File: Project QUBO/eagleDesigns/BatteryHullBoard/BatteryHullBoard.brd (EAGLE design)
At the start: 53.3 x 39.7 mm, 7 parts, among them U1 KSK-1E66, U2 CMXSIPSSR

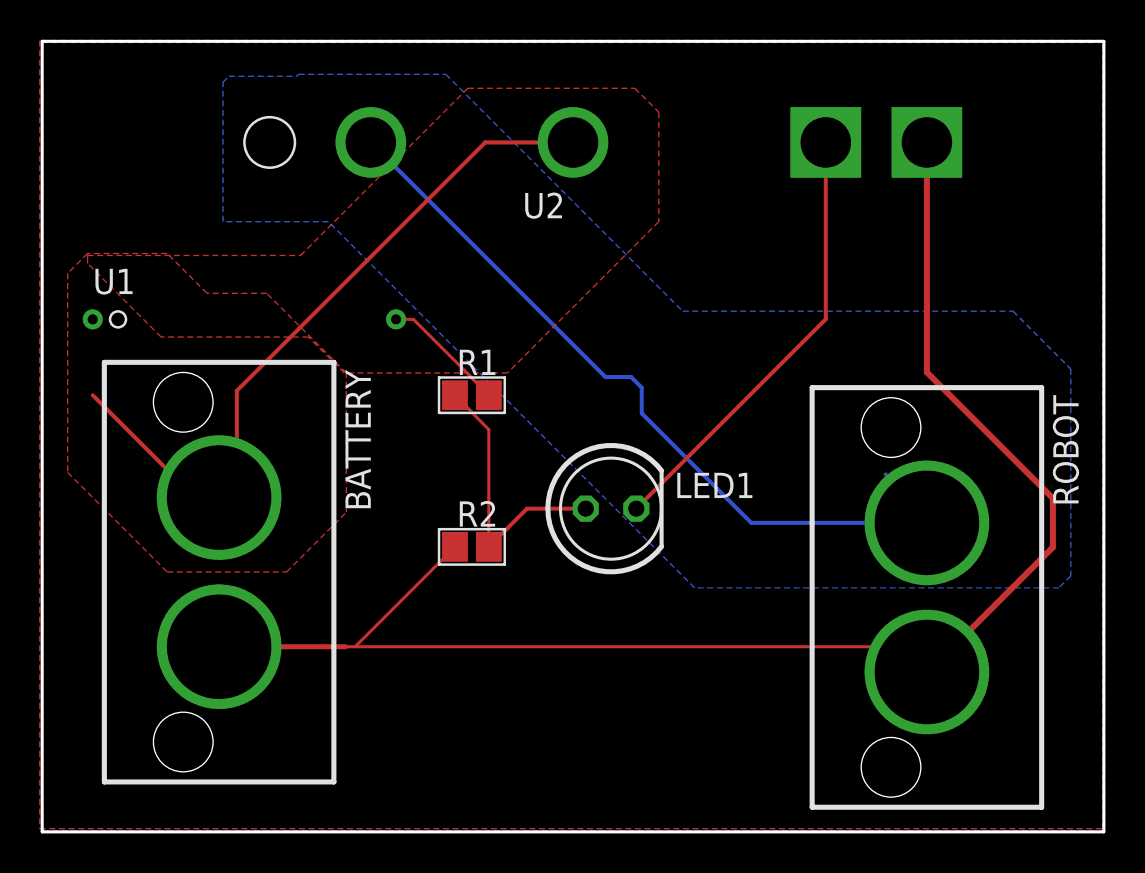
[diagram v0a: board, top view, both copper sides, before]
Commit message: 
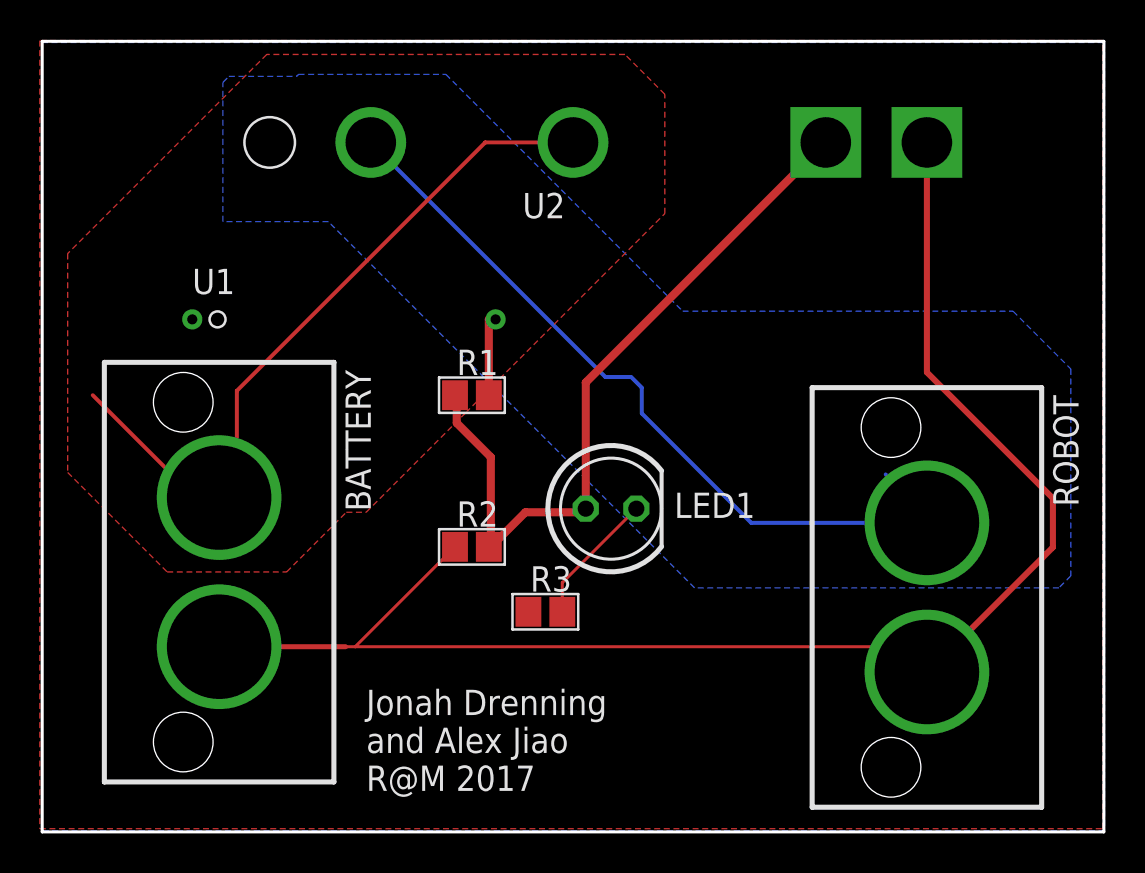
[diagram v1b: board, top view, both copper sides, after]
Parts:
- added R3: 10000, resistor:R0805
- moved U1 5.00 mm to (60.9, 59.7)
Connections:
- removed net N$6: LED1.K, U2.P$3
- new net N$4: LED1.K, R3.2
- net GND: now also R3.1
- net N$3: now also U2.P$3
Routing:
- net N$3: track 14.0 -> 37.4 mm
- net N$6: track 22.3 -> 0.00 mm
- net N$4: track 0.00 -> 6.72 mm
- net N$1: track 6.25 -> 4.15 mm
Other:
- board text added: "Jonah Drenning and Alex Jiao R@M 2017"
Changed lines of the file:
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@@
 <wire x1="45.72" y1="73.66" x2="99.06" y2="73.66" width="0.1524" layer="20"/>
 <wire x1="99.06" y1="73.66" x2="99.06" y2="33.94" width="0.1524" layer="20"/>
+<text x="62" y="36" size="1.27" layer="21">Jonah Drenning
+and Alex Jiao
+R@M 2017</text>
 </plain>
 <attributes>
@@
 <elements>
 <element name="BATTERY" library="molex" package="SUPERSABRE_2CIRCUIT" value="2_SUPERSABRE" x="54.61" y="46.99" rot="R270"/>
-<element name="LED1" library="led" package="LED5MM" value="" x="74.3" y="50.18"/>
-<element name="R1" library="resistor" package="R0805" value="1000" x="67.31" y="55.88"/>
-<element name="R2" library="resistor" package="R0805" value="7700" x="67.31" y="48.26"/>
+<element name="LED1" library="led" package="LED5MM" value="" x="74.3" y="50.18" smashed="yes">
+<attribute name="NAME" x="77.475" y="49.7134" size="1.27" layer="25" ratio="10"/>
+<attribute name="VALUE" x="77.5004" y="48.3766" size="1.27" layer="27" ratio="10"/>
+</element>
+<element name="R1" library="resistor" package="R0805" value="1000" x="67.31" y="55.88" smashed="yes">
+<attribute name="NAME" x="66.548" y="56.896" size="1.27" layer="25"/>
+<attribute name="VALUE" x="69.548" y="55.594" size="1.27" layer="27"/>
+</element>
+<element name="R2" library="resistor" package="R0805" value="7700" x="67.31" y="48.26" smashed="yes">
+<attribute name="NAME" x="66.548" y="49.276" size="1.27" layer="25"/>
+<attribute name="VALUE" x="64.548" y="45.974" size="1.27" layer="27"/>
+</element>
 <element name="ROBOT" library="molex" package="SUPERSABRE_2CIRCUIT" value="2_SUPERSABRE" x="90.17" y="45.72" rot="R270"/>
-<element name="U1" library="KSK-1E66" package="KSK-1E66" value="KSK-1E66" x="55.88" y="59.69"/>
+<element name="U1" library="KSK-1E66" package="KSK-1E66" value="KSK-1E66" x="60.88" y="59.69"/>
 <element name="U2" library="CMXSIPSSR" package="CMXSIPSSR" value="CMXSIPSSR" x="76.2" y="67.31"/>
+<element name="R3" library="resistor" package="R0805" value="10000" x="71" y="45" smashed="yes">
+<attribute name="NAME" x="70.238" y="46.016" size="1.27" layer="25"/>
+<attribute name="VALUE" x="68.238" y="42.714" size="1.27" layer="27"/>
+</element>
 </elements>
 <signals>
@@
 <contactref element="R1" pad="1"/>
 <contactref element="LED1" pad="A"/>
-<wire x1="67.2814" y1="55.0353125" x2="67.2814" y2="55.0586" width="0.1524" layer="1"/>
-<wire x1="67.2814" y1="55.0586" x2="66.46" y2="55.88" width="0.1524" layer="1"/>
-<wire x1="68.16" y1="48.26" x2="68.16" y2="54.1567125" width="0.1524" layer="1"/>
-<wire x1="68.16" y1="54.1567125" x2="67.2814" y2="55.0353125" width="0.1524" layer="1"/>
-<wire x1="73.03" y1="50.18" x2="70.08" y2="50.18" width="0.2" layer="1"/>
-<wire x1="70.08" y1="50.18" x2="68.16" y2="48.26" width="0.2" layer="1"/>
+<contactref element="U2" pad="P$3"/>
+<wire x1="85.09" y1="68.58" x2="73.03" y2="56.52" width="0.4064" layer="1"/>
+<wire x1="73.03" y1="56.52" x2="73.03" y2="50.18" width="0.4064" layer="1"/>
+<wire x1="73.03" y1="50.18" x2="72.85" y2="50" width="0.4064" layer="1"/>
+<wire x1="70" y1="50" x2="72.85" y2="50" width="0.4064" layer="1"/>
+<wire x1="68.26" y1="48.26" x2="70" y2="50" width="0.4064" layer="1"/>
+<wire x1="68.26" y1="48.26" x2="68.16" y2="48.26" width="0.4064" layer="1"/>
+<wire x1="66.46" y1="55.88" x2="66.548" y2="55.792" width="0.4064" layer="1"/>
+<wire x1="66.548" y1="55.792" x2="66.548" y2="54.483" width="0.4064" layer="1"/>
+<wire x1="66.548" y1="54.483" x2="68.26" y2="52.771" width="0.4064" layer="1"/>
+<wire x1="68.26" y1="52.771" x2="68.26" y2="48.26" width="0.4064" layer="1"/>
 </signal>
 <signal name="PWR2">
@@
 <wire x1="90.17" y1="49.83" x2="88.1" y2="51.9" width="0.2" layer="16"/>
 </signal>
-<signal name="N$6">
-<contactref element="LED1" pad="K"/>
-<contactref element="U2" pad="P$3"/>
-<wire x1="85.09" y1="68.58" x2="85.09" y2="59.7" width="0.2" layer="1"/>
-<wire x1="85.09" y1="59.7" x2="75.57" y2="50.18" width="0.2" layer="1"/>
-</signal>
 <signal name="GND">
 <contactref element="R2" pad="1"/>
 <contactref element="BATTERY" pad="P$2"/>
-<contactref element="ROBOT" pad="P$2"/>
 <wire x1="54.61" y1="43.2435" x2="60.96" y2="43.2435" width="0.254" layer="1"/>
 <wire x1="60.96" y1="43.2435" x2="61.4435" y2="43.2435" width="0.1524" layer="1"/>
@@
 <wire x1="61.4435" y1="43.2435" x2="88.8365" y2="43.2435" width="0.1524" layer="1"/>
 <wire x1="90.17" y1="41.91" x2="88.8365" y2="43.2435" width="0.1524" layer="1"/>
-<wire x1="90.17" y1="41.91" x2="90.17" y2="41.9735" width="0.1524" layer="1"/>
 <contactref element="U2" pad="P$4"/>
 <wire x1="90.17" y1="68.58" x2="90.17" y2="57.03" width="0.3048" layer="1"/>
@@
 <vertex x="99" y="73.7"/>
 </polygon>
+<contactref element="ROBOT" pad="P$2"/>
+<contactref element="R3" pad="1"/>
 </signal>
 <signal name="PWR1">
-<polygon width="0.2" layer="1" isolate="0.00030625" thermals="no">
-<vertex x="52" y="47"/>
-<vertex x="58" y="47"/>
-<vertex x="61" y="50"/>
-<vertex x="61" y="57"/>
-<vertex x="57" y="61"/>
-<vertex x="54" y="61"/>
-<vertex x="52" y="63"/>
-<vertex x="48" y="63"/>
-<vertex x="47" y="62"/>
-<vertex x="47" y="52"/>
-</polygon>
 <contactref element="BATTERY" pad="P$1"/>
 <wire x1="48.26" y1="55.88" x2="52.07" y2="52.07" width="0.2" layer="1"/>
@@
 <wire x1="55.5" y1="56.1" x2="55.5" y2="51.6265" width="0.2" layer="1"/>
 <wire x1="55.5" y1="51.6265" x2="54.61" y2="50.7365" width="0.2" layer="1"/>
-<polygon width="0.2" layer="1" isolate="0.00030625" thermals="no">
-<vertex x="48" y="62.9"/>
-<vertex x="58.7" y="62.9"/>
-<vertex x="67.1" y="71.3"/>
-<vertex x="75.5" y="71.3"/>
-<vertex x="76.7" y="70.1"/>
-<vertex x="76.7" y="64.6"/>
-<vertex x="73.6" y="61.5"/>
-<vertex x="69.1" y="57"/>
-<vertex x="60.9" y="57"/>
-<vertex x="59.1" y="58.8"/>
-<vertex x="51.7" y="58.8"/>
-<vertex x="48" y="62.5"/>
-<vertex x="48" y="62.8"/>
+<polygon width="0.4064" layer="1" orphans="yes" thermals="no">
+<vertex x="47" y="52"/>
+<vertex x="52" y="47"/>
+<vertex x="58" y="47"/>
+<vertex x="61" y="50"/>
+<vertex x="62" y="50"/>
+<vertex x="67" y="55"/>
+<vertex x="77" y="65"/>
+<vertex x="77" y="71"/>
+<vertex x="75" y="73"/>
+<vertex x="57" y="73"/>
+<vertex x="47" y="63"/>
 </polygon>
 </signal>
@@
 <contactref element="U1" pad="P$2"/>
 <contactref element="R1" pad="2"/>
-<wire x1="67.3386" y1="56.7246875" x2="67.3386" y2="56.7014" width="0.1524" layer="1"/>
-<wire x1="67.3386" y1="56.7014" x2="68.16" y2="55.88" width="0.1524" layer="1"/>
-<wire x1="64.3732875" y1="59.69" x2="63.5" y2="59.69" width="0.1524" layer="1"/>
-<wire x1="64.3732875" y1="59.69" x2="67.3386" y2="56.7246875" width="0.1524" layer="1"/>
+<wire x1="68.5" y1="59.69" x2="68.16" y2="59.69" width="0.4064" layer="1"/>
+<wire x1="68.16" y1="59.69" x2="68.16" y2="55.88" width="0.4064" layer="1"/>
+</signal>
+<signal name="N$4">
+<contactref element="LED1" pad="K"/>
+<contactref element="R3" pad="2"/>
+<wire x1="71.85" y1="45" x2="71.85" y2="46.46" width="0.1524" layer="1"/>
+<wire x1="71.85" y1="46.46" x2="75.57" y2="50.18" width="0.1524" layer="1"/>
 </signal>
 </signals>
 </board>
 </drawing>
+<compatibility>
+<note version="6.3" minversion="6.2.2" severity="warning">
+Since Version 6.2.2 text objects can contain more than one line,
+which will not be processed correctly with this version.
+</note>
+</compatibility>
 </eagle>
